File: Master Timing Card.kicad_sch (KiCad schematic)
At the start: 27 parts, among them CN1 Samtec GRF1-J-P-08-E-RA-TH1, CN2 Amphenol 86093488613755E1LF, U1 Analog MAX3483ESA+, U2 DS2431P+

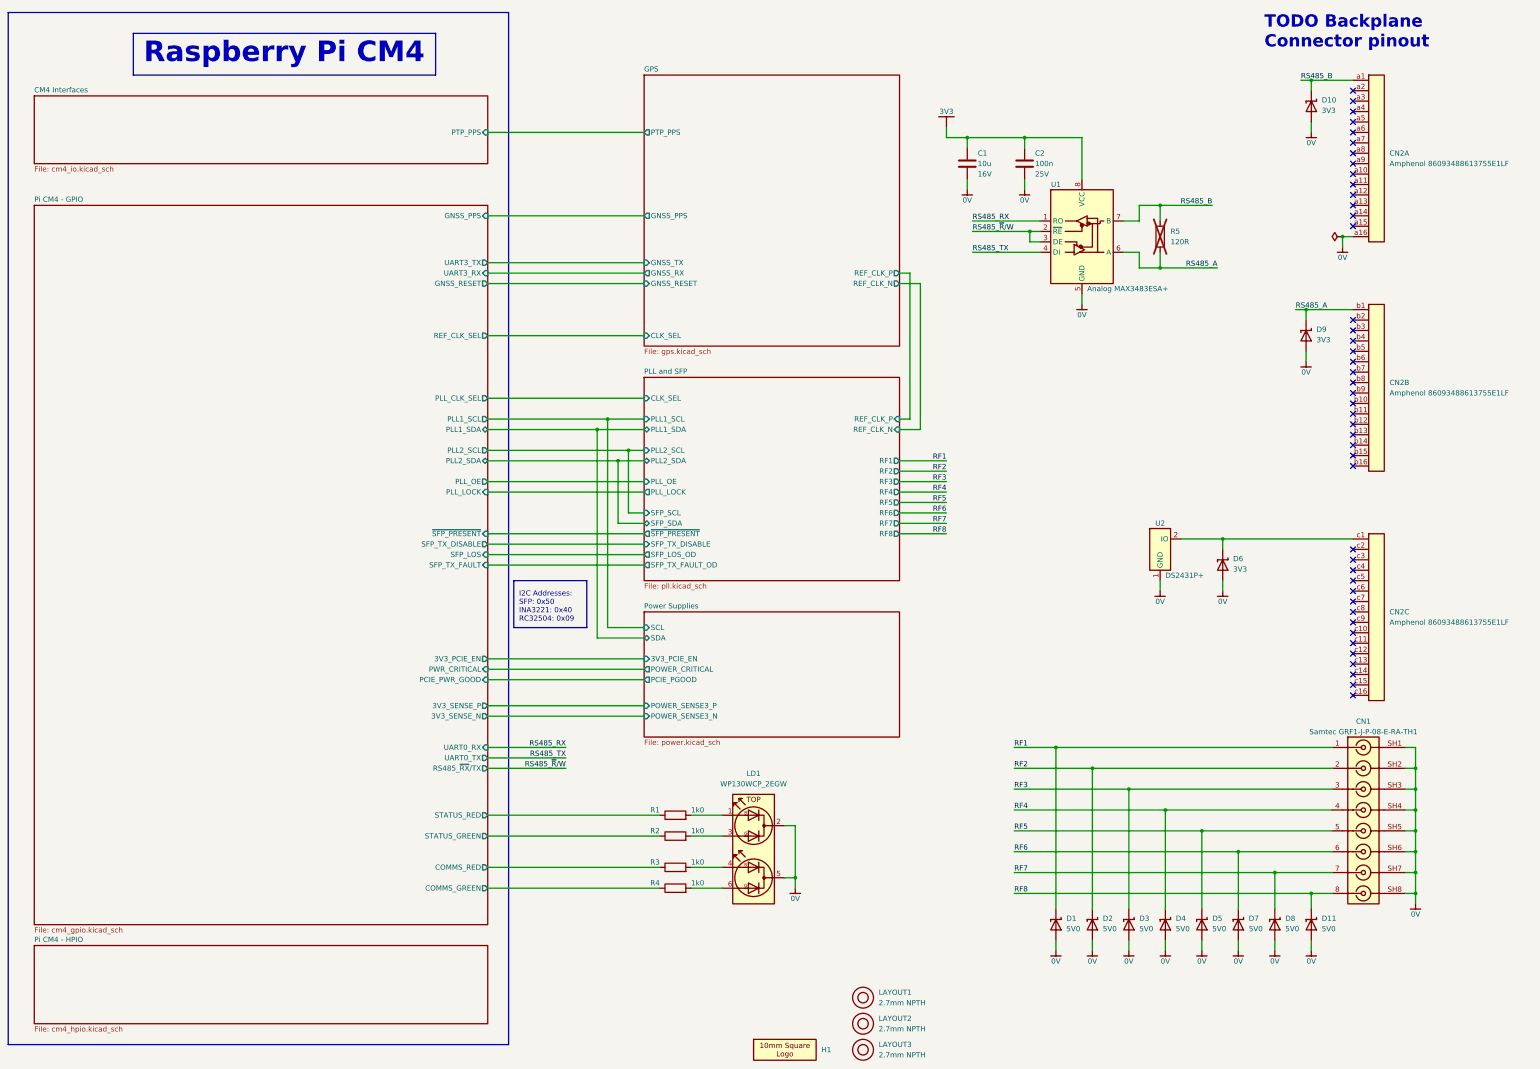
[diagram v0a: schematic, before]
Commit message: Fixed connector offsets
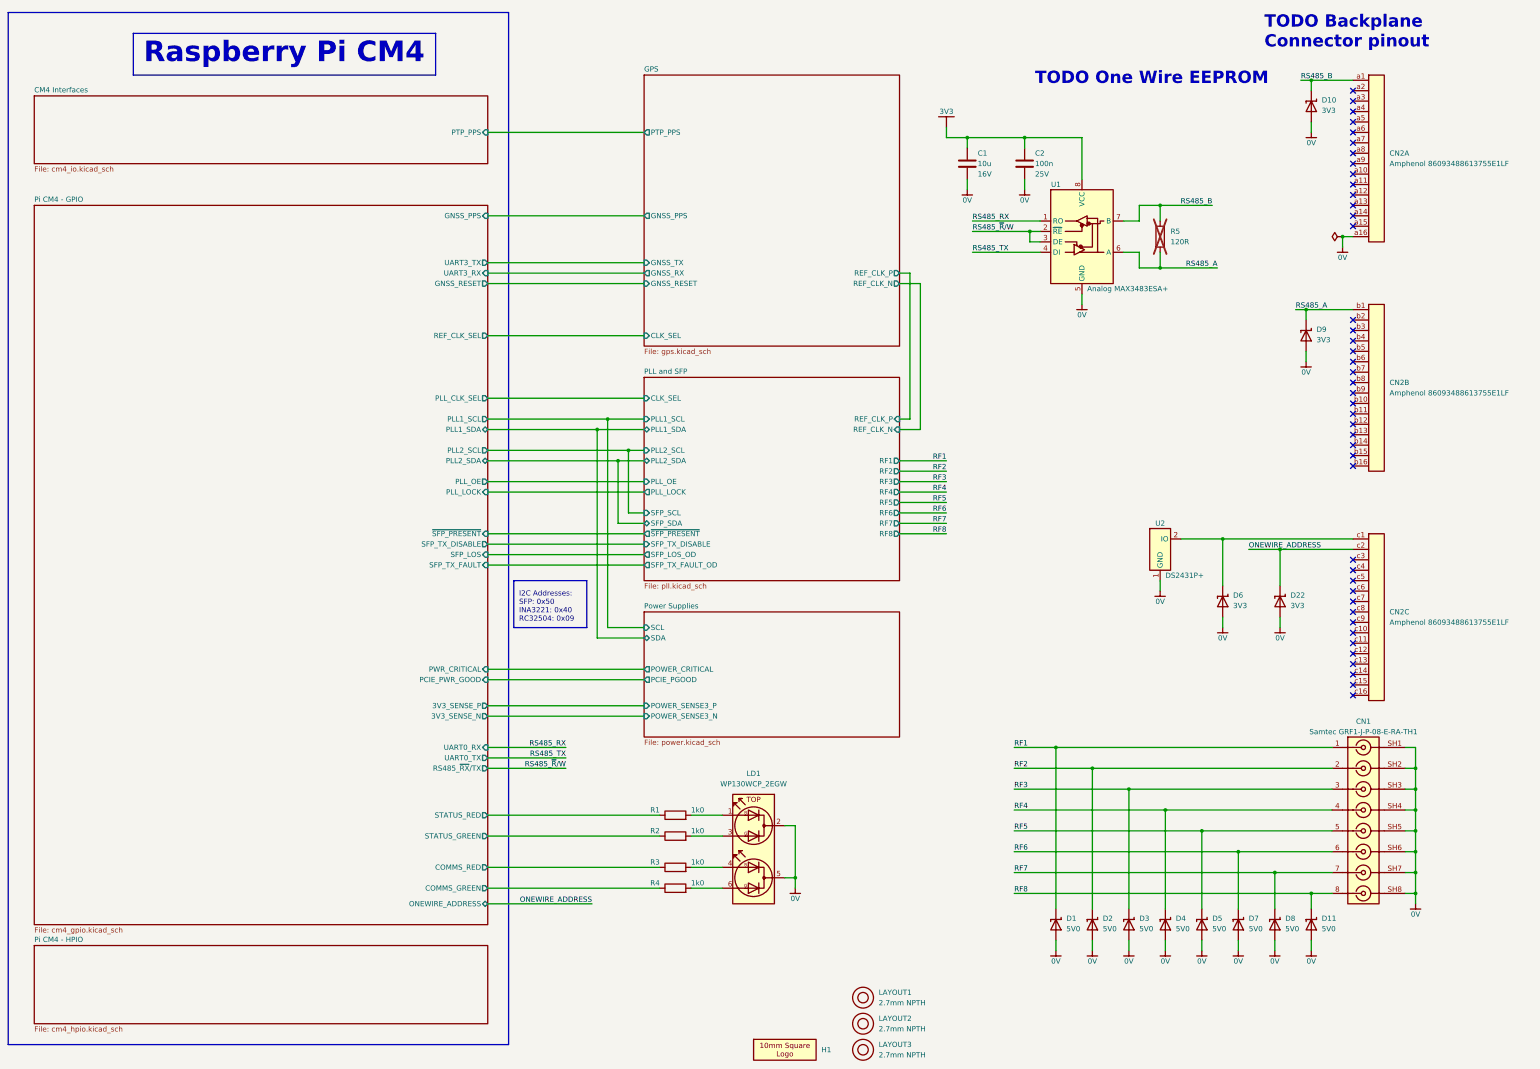
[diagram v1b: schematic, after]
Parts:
- added D22: 3V3, Diode_SMD:D_SOD-523, symbol AAA_Preferred_WUT:nexperia PESD3V3U1UB,115
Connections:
- net 0V: now also D22.2 (A)
- net ONEWIRE_ADDRESS: now reaches CN2.c2
- net ONEWIRE_ADDRESS: now also D22.1 (K)
- no-connect marks 44 -> 43
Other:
- sheet Pi CM4 - GPIO ports: added ONEWIRE_ADDRESS; removed 3V3_PCIE_EN
- sheet Power Supplies ports: added none; removed 3V3_PCIE_EN
- note added: "TODO One Wire EEPROM"
- moved on the sheet: D6
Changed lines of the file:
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@@
   (junction (at 278.13 49.53) (diameter 0.9144) (color 0 0 0 0)
+  )
+  (junction (at 340.36 149.86) (diameter 0) (color 0 0 0 0)
   )
   (junction (at 346.71 91.44) (diameter 0) (color 0 0 0 0)
@@
   (no_connect (at 358.14 182.88))
   (no_connect (at 358.14 119.38))
-  (no_connect (at 358.14 149.86))
   (no_connect (at 358.14 60.96))
   (no_connect (at 358.14 45.72))
@@
     (stroke (width 0) (type default))
   )
+  (wire (pts (xy 332.74 149.86) (xy 340.36 149.86))
+    (stroke (width 0) (type default))
+  )
   (wire (pts (xy 278.13 59.69) (xy 278.13 62.23))
     (stroke (width 0) (type solid))
@@
     (stroke (width 0) (type default))
   )
-  (wire (pts (xy 326.39 147.32) (xy 326.39 149.86))
+  (wire (pts (xy 326.39 147.32) (xy 326.39 158.75))
     (stroke (width 0) (type default))
   )
@@
     (stroke (width 0) (type default))
   )
+  (wire (pts (xy 147.32 236.22) (xy 172.72 236.22))
+    (stroke (width 0) (type default))
+  )
   (wire (pts (xy 176.53 118.11) (xy 185.42 118.11))
+    (stroke (width 0) (type default))
+  )
+  (wire (pts (xy 340.36 158.75) (xy 340.36 149.86))
     (stroke (width 0) (type default))
   )
@@
     (stroke (width 0) (type default))
   )
+  (wire (pts (xy 340.36 166.37) (xy 340.36 168.91))
+    (stroke (width 0) (type default))
+  )
+  (wire (pts (xy 340.36 149.86) (xy 358.14 149.86))
+    (stroke (width 0) (type default))
+  )
   (wire (pts (xy 147.32 135.89) (xy 185.42 135.89))
     (stroke (width 0) (type default))
@@
     (stroke (width 0) (type default))
   )
-  (wire (pts (xy 147.32 176.53) (xy 185.42 176.53))
-    (stroke (width 0) (type default))
-  )
   (wire (pts (xy 176.53 118.11) (xy 176.53 168.91))
     (stroke (width 0) (type default))
@@
     (stroke (width 0) (type default))
   )
-  (wire (pts (xy 326.39 157.48) (xy 326.39 160.02))
+  (wire (pts (xy 326.39 166.37) (xy 326.39 168.91))
     (stroke (width 0) (type default))
   )
@@
     )
   )
+  (text "TODO One Wire EEPROM" (at 280.67 36.83 0)
+    (effects (font (size 3 3) (thickness 0.6) bold (color 255 0 0 1)) (justify left bottom))
+  )
   (text "TODO Backplane\nConnector pinout	" (at 336.55 27.94 0)
     (effects (font (size 3 3) (thickness 0.6) bold (color 255 0 0 1)) (justify left bottom))
@@
     (effects (font (size 1.27 1.27)) (justify right bottom))
   )
+  (label "ONEWIRE_ADDRESS" (at 332.74 149.86 0) (fields_autoplaced)
+    (effects (font (size 1.27 1.27)) (justify left bottom))
+  )
   (label "RS485_A" (at 325.12 81.28 180) (fields_autoplaced)
     (effects (font (size 1.27 1.27)) (justify right bottom))
@@
   (label "RF2" (at 275.59 203.2 0) (fields_autoplaced)
     (effects (font (size 1.27 1.27)) (justify left bottom))
+  )
+  (label "ONEWIRE_ADDRESS" (at 172.72 236.22 180) (fields_autoplaced)
+    (effects (font (size 1.27 1.27)) (justify right bottom))
   )
   (label "RF5" (at 275.59 218.44 0) (fields_autoplaced)
@@
     )
   )
+  (symbol (lib_id "AAA_Preferred_WUT:nexperia PESD3V3U1UB,115") (at 340.36 162.56 90) (unit 1)
+    (in_bom yes) (on_board yes) (dnp no) (fields_autoplaced)
+    (property "Reference" "D22" (at 342.9 161.036 90)
+      (effects (font (size 1.27 1.27)) (justify right))
+    )
+    (property "Value" "3V3" (at 342.9 163.576 90)
+      (effects (font (size 1.27 1.27)) (justify right))
+    )
+    (property "Footprint" "Diode_SMD:D_SOD-523" (at 340.36 162.56 0)
+      (effects (font (size 1.27 1.27)) hide)
+    )
+    (property "Datasheet" "https://www.mouser.co.uk/datasheet/2/916/PESD3V3U1UB-2938348.pdf" (at 340.36 162.56 0)
+      (effects (font (size 1.27 1.27)) hide)
+    )
+    (property "Manufacturer" "nexperia" (at 340.36 162.56 0)
+      (effects (font (size 1.27 1.27)) hide)
+    )
+    (property "MPN" "PESD3V3U1UB,115" (at 340.36 162.56 0)
+      (effects (font (size 1.27 1.27)) hide)
+    )
+    (property "Height" "0.65mm" (at 340.36 162.56 0)
+      (effects (font (size 1.27 1.27)) hide)
+    )
+    (pin "2")
+    (pin "1")
+    (instances
+      (project "Master Timing Card"
+        (path "/6e8e281e-e30f-459d-852f-231836068db5"
+          (reference "D22") (unit 1)
+        )
+      )
+    )
+  )
   (symbol (lib_id "Power_WUT:0V") (at 303.53 247.65 0) (unit 1)
     (in_bom no) (on_board no) (dnp no)
@@
     )
   )
-  (symbol (lib_id "Power_WUT:0V") (at 326.39 160.02 0) (unit 1)
+  (symbol (lib_id "Power_WUT:0V") (at 326.39 168.91 0) (unit 1)
     (in_bom no) (on_board no) (dnp no)
-    (property "Reference" "#PWR012" (at 326.39 160.02 0)
-      (effects (font (size 1.27 1.27)) hide)
-    )
-    (property "Value" "0V" (at 326.39 162.56 0) (do_not_autoplace)
+    (property "Reference" "#PWR012" (at 326.39 168.91 0)
+      (effects (font (size 1.27 1.27)) hide)
+    )
+    (property "Value" "0V" (at 326.39 171.45 0) (do_not_autoplace)
       (effects (font (size 1.27 1.27)))
     )
-    (property "Footprint" "" (at 326.39 160.02 0)
-      (effects (font (size 1.27 1.27)) hide)
-    )
-    (property "Datasheet" "" (at 326.39 160.02 0)
+    (property "Footprint" "" (at 326.39 168.91 0)
+      (effects (font (size 1.27 1.27)) hide)
+    )
+    (property "Datasheet" "" (at 326.39 168.91 0)
       (effects (font (size 1.27 1.27)) hide)
     )
@@
     )
   )
+  (symbol (lib_id "Power_WUT:0V") (at 340.36 168.91 0) (unit 1)
+    (in_bom no) (on_board no) (dnp no)
+    (property "Reference" "#PWR0272" (at 340.36 168.91 0)
+      (effects (font (size 1.27 1.27)) hide)
+    )
+    (property "Value" "0V" (at 340.36 171.45 0) (do_not_autoplace)
+      (effects (font (size 1.27 1.27)))
+    )
+    (property "Footprint" "" (at 340.36 168.91 0)
+      (effects (font (size 1.27 1.27)) hide)
+    )
+    (property "Datasheet" "" (at 340.36 168.91 0)
+      (effects (font (size 1.27 1.27)) hide)
+    )
+    (pin "1")
+    (instances
+      (project "Master Timing Card"
+        (path "/6e8e281e-e30f-459d-852f-231836068db5"
+          (reference "#PWR0272") (unit 1)
+        )
+      )
+    )
+  )
   (symbol (lib_id "AAA_Preferred_WUT:KOA Speer RK73H1ETTP1001F") (at 193.04 227.33 90) (unit 1)
     (in_bom yes) (on_board yes) (dnp no)
@@
     )
   )
-  (symbol (lib_id "AAA_Preferred_WUT:nexperia PESD3V3U1UB,115") (at 326.39 153.67 90) (unit 1)
+  (symbol (lib_id "AAA_Preferred_WUT:nexperia PESD3V3U1UB,115") (at 326.39 162.56 90) (unit 1)
     (in_bom yes) (on_board yes) (dnp no) (fields_autoplaced)
-    (property "Reference" "D6" (at 328.93 152.146 90)
-      (effects (font (size 1.27 1.27)) (justify right))
-    )
-    (property "Value" "3V3" (at 328.93 154.686 90)
-      (effects (font (size 1.27 1.27)) (justify right))
-    )
-    (property "Footprint" "Diode_SMD:D_SOD-523" (at 326.39 153.67 0)
-      (effects (font (size 1.27 1.27)) hide)
-    )
-    (property "Datasheet" "https://www.mouser.co.uk/datasheet/2/916/PESD3V3U1UB-2938348.pdf" (at 326.39 153.67 0)
-      (effects (font (size 1.27 1.27)) hide)
-    )
-    (property "Manufacturer" "nexperia" (at 326.39 153.67 0)
-      (effects (font (size 1.27 1.27)) hide)
-    )
-    (property "MPN" "PESD3V3U1UB,115" (at 326.39 153.67 0)
-      (effects (font (size 1.27 1.27)) hide)
-    )
-    (property "Height" "0.65mm" (at 326.39 153.67 0)
+    (property "Reference" "D6" (at 328.93 161.036 90)
+      (effects (font (size 1.27 1.27)) (justify right))
+    )
+    (property "Value" "3V3" (at 328.93 163.576 90)
+      (effects (font (size 1.27 1.27)) (justify right))
+    )
+    (property "Footprint" "Diode_SMD:D_SOD-523" (at 326.39 162.56 0)
+      (effects (font (size 1.27 1.27)) hide)
+    )
+    (property "Datasheet" "https://www.mouser.co.uk/datasheet/2/916/PESD3V3U1UB-2938348.pdf" (at 326.39 162.56 0)
+      (effects (font (size 1.27 1.27)) hide)
+    )
+    (property "Manufacturer" "nexperia" (at 326.39 162.56 0)
+      (effects (font (size 1.27 1.27)) hide)
+    )
+    (property "MPN" "PESD3V3U1UB,115" (at 326.39 162.56 0)
+      (effects (font (size 1.27 1.27)) hide)
+    )
+    (property "Height" "0.65mm" (at 326.39 162.56 0)
       (effects (font (size 1.27 1.27)) hide)
     )
@@
       (effects (font (size 1.27 1.27)) (justify right))
     )
-    (pin "3V3_PCIE_EN" output (at 147.32 176.53 0)
-      (effects (font (size 1.27 1.27)) (justify right))
-    )
     (pin "GNSS_RESET" output (at 147.32 85.09 0)
       (effects (font (size 1.27 1.27)) (justify right))
@@
     )
     (pin "PLL_CLK_SEL" output (at 147.32 113.03 0)
+      (effects (font (size 1.27 1.27)) (justify right))
+    )
+    (pin "ONEWIRE_ADDRESS" bidirectional (at 147.32 236.22 0)
       (effects (font (size 1.27 1.27)) (justify right))
     )
@@
       (effects (font (size 1.27 1.27)) (justify left))
     )
-    (pin "3V3_PCIE_EN" input (at 185.42 176.53 180)
-      (effects (font (size 1.27 1.27)) (justify left))
-    )

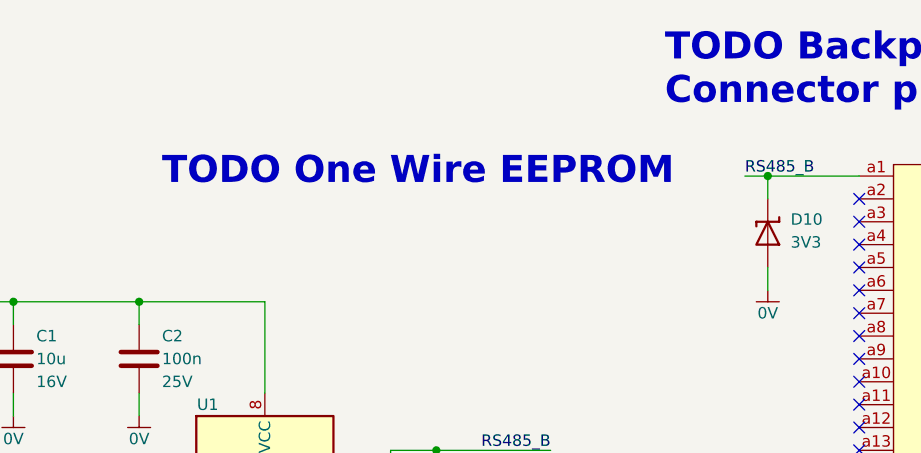
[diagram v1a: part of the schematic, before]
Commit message: Think complete - apart from 12V connection
Removed accidential step file
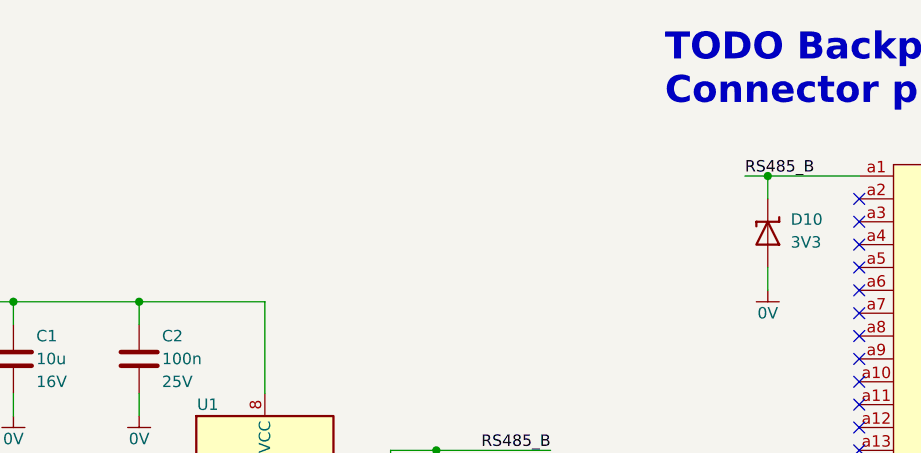
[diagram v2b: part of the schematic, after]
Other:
- note removed: "TODO One Wire EEPROM"
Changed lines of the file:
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@@
     )
-  )
-  (text "TODO One Wire EEPROM" (at 280.67 36.83 0)
-    (effects (font (size 3 3) (thickness 0.6) bold (color 255 0 0 1)) (justify left bottom))
   )
   (text "TODO Backplane\nConnector pinout	" (at 336.55 27.94 0)
